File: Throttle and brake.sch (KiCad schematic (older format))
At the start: 9 parts, among them P2 Throttle Pedal, U1 Amplifier, U2 ADUC816

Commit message: version from flash drive
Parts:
- removed R3: Pot, symbol POT
- removed U2: ADUC816, symbol ADUC816
- added C? (x2): CP1, symbol CP1
- added P3: Pot connector, Connect:bornier3, symbol CONN_01X03
- added Q?: Q_PNP_BCE, symbol Q_PNP_BCE
- added R? (x2): R, symbol R
- added U2: Teensy_3.2, symbol Teensy_3.2
- 10k1, P2: footprint (none) -> Connect:bornier3
- 3P1: renamed from .2; footprint (none) -> Connect:bornier3
- 4P1: renamed from .; footprint (none) -> Connect:bornier4
- R1, R2: footprint (none) -> Resistors_SMD:R_1210_HandSoldering
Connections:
- net labels added: Brakesignal, GNDREF, Throttlesignal
- wire segments 47 -> 44
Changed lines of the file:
@@
 LIBS:contrib
 LIBS:valves
+LIBS:electric_car
 LIBS:Throttle and brake-cache
 EELAYER 25 0
@@
 $EndDescr
 $Comp
-L POT R3
-U 1 1 57F328A6
-P 3150 2000
-F 0 "R3" H 3150 1920 50  0000 C CNN
-F 1 "Pot" H 3150 2000 50  0000 C CNN
-F 2 "" H 3150 2000 50  0000 C CNN
-F 3 "" H 3150 2000 50  0000 C CNN
-	1    3150 2000
-	0    1    1    0
-$EndComp
-$Comp
 L R_Small R1
 U 1 1 57F33006
@@
 F 0 "R1" H 2280 3120 50  0000 L CNN
 F 1 "1k" H 2280 3060 50  0000 L CNN
-F 2 "" H 2250 3100 50  0000 C CNN
+F 2 "Resistors_SMD:R_1210_HandSoldering" H 2250 3100 50  0001 C CNN
 F 3 "" H 2250 3100 50  0000 C CNN
 	1    2250 3100
@@
 F 0 "R2" H 2280 3520 50  0000 L CNN
 F 1 "1k" H 2280 3460 50  0000 L CNN
-F 2 "" H 2250 3500 50  0000 C CNN
+F 2 "Resistors_SMD:R_1210_HandSoldering" H 2250 3500 50  0001 C CNN
 F 3 "" H 2250 3500 50  0000 C CNN
 	1    2250 3500
@@
 F 0 "10k1" H 1950 3270 50  0000 C CNN
 F 1 "POT" H 1950 3350 50  0000 C CNN
-F 2 "" H 1950 3350 50  0000 C CNN
+F 2 "Connect:bornier3" H 1950 3350 50  0001 C CNN
 F 3 "" H 1950 3350 50  0000 C CNN
 	1    1950 3350
@@
 F 0 "U1" H 3900 3500 50  0000 L CNN
 F 1 "Amplifier" H 3900 3050 50  0000 L CNN
-F 2 "" H 3950 3300 50  0000 C CNN
+F 2 "" H 3950 3300 50  0001 C CNN
 F 3 "" H 3950 3300 50  0000 C CNN
 	1    3950 3300
-	1    0    0    -1
-$EndComp
-$Comp
-L ADUC816 U2
-U 1 1 57F33F31
-P 7250 2800
-F 0 "U2" H 6300 4600 50  0000 L CNN
-F 1 "ADUC816" H 6300 4500 50  0000 L CNN
-F 2 "" H 7250 2600 50  0000 C CNN
-F 3 "" H 7250 2600 50  0000 C CNN
-	1    7250 2800
 	1    0    0    -1
 $EndComp
@@
 	1    0    0    -1
 $EndComp
-Wire Notes Line
-	3300 1750 3000 1750
-Wire Notes Line
-	3300 2250 3300 1750
-Wire Notes Line
-	3000 2250 3300 2250
-Wire Notes Line
-	3000 1750 3000 2250
 Connection ~ 2550 2850
 Wire Wire Line
 	3850 2850 3850 3000
-Wire Wire Line
-	5550 1600 6150 1600
-Wire Wire Line
-	5550 3300 5550 1600
-Wire Wire Line
-	4250 3300 5550 3300
-Wire Wire Line
-	5300 1500 6150 1500
-Wire Wire Line
-	5300 2000 5300 1500
-Wire Wire Line
-	3300 2000 5300 2000
 Connection ~ 1950 1650
 Connection ~ 1950 2850
@@
 	1950 3750 1950 3500
 Wire Wire Line
-	2550 3750 2250 3750
-Wire Wire Line
-	2250 3750 1950 3750
-Wire Wire Line
-	2550 3600 2550 3750
+	1950 3750 2550 3750
+Wire Wire Line
+	2550 3750 2550 3600
 Connection ~ 2550 3000
 Wire Wire Line
 	1950 2850 1950 3200
 Wire Wire Line
-	1650 2850 1950 2850
-Wire Wire Line
-	1950 2850 2550 2850
-Wire Wire Line
-	2550 2850 3850 2850
+	1650 2850 3850 2850
 Wire Wire Line
 	2550 2850 2550 3000
 Connection ~ 2250 3350
 Wire Wire Line
-	2250 3000 2550 3000
-Wire Wire Line
-	2550 3000 2800 3000
-Wire Wire Line
-	2250 3600 2550 3600
-Wire Wire Line
-	2550 3600 2800 3600
-Wire Wire Line
-	2250 3200 2250 3350
-Wire Wire Line
-	2250 3350 2250 3400
-Wire Wire Line
-	3150 2400 3150 2150
-Wire Wire Line
-	1950 2400 2550 2400
-Wire Wire Line
-	2550 2400 3150 2400
-Wire Wire Line
-	3150 1650 3150 1850
-Wire Wire Line
-	1650 1650 1950 1650
-Wire Wire Line
-	1950 1650 3150 1650
+	2250 3000 2800 3000
+Wire Wire Line
+	2250 3600 2800 3600
+Wire Wire Line
+	2250 3200 2250 3400
+Wire Wire Line
+	3150 2100 3150 2400
+Wire Wire Line
+	3150 2400 1950 2400
+Wire Wire Line
+	3150 1650 3150 1900
+Wire Wire Line
+	1650 1650 3150 1650
 Connection ~ 100  450
 $Comp
@@
 Jean, Fred. Euphraim
 $Comp
-L CONN_01X03 .2
+L CONN_01X03 3P1
 U 1 1 57F357A4
 P 4500 4850
-F 0 ".2" H 4500 5150 50  0000 C CNN
+F 0 "3P1" H 4500 5150 50  0000 C CNN
 F 1 "Lever" V 4600 4850 50  0000 C CNN
-F 2 "" H 4500 4850 50  0000 C CNN
+F 2 "Connect:bornier3" H 4500 4850 50  0001 C CNN
 F 3 "" H 4500 4850 50  0000 C CNN
 	1    4500 4850
@@
 	4250 4850 4300 4850
 $Comp
-L CONN_01X04 .
+L CONN_01X04 4P1
 U 1 1 580590EC
 P 2600 4850
-F 0 "." H 2600 5100 50  0000 C CNN
+F 0 "4P1" H 2600 5100 50  0000 C CNN
 F 1 "Ignition Switch" V 2700 4850 50  0000 C CNN
-F 2 "" H 2600 4850 50  0000 C CNN
+F 2 "Connect:bornier4" H 2600 4850 50  0001 C CNN
 F 3 "" H 2600 4850 50  0000 C CNN
 	1    2600 4850
@@
 F 0 "P2" H 3000 3500 35  0000 C CNN
 F 1 "Throttle Pedal" V 3100 3300 50  0000 C CNN
-F 2 "" H 3000 3300 50  0000 C CNN
+F 2 "Connect:bornier3" H 3000 3300 50  0001 C CNN
 F 3 "" H 3000 3300 50  0000 C CNN
 	1    3000 3300
@@
 $EndComp
 Wire Wire Line
-	2100 3350 2250 3350
-Wire Wire Line
-	2250 3350 2650 3350
+	2100 3350 2650 3350
 Wire Wire Line
 	2650 3350 2650 3550
@@
 Wire Wire Line
 	2800 3600 2800 3400
+$Comp
+L CONN_01X03 P3
+U 1 1 580ECAE0
+P 3350 2000
+F 0 "P3" H 3350 2200 50  0000 C CNN
+F 1 "Pot connector" V 3450 2000 50  0000 C CNN
+F 2 "Connect:bornier3" H 3350 2000 50  0001 C CNN
+F 3 "" H 3350 2000 50  0000 C CNN
+	1    3350 2000
+	1    0    0    -1
+$EndComp
+Wire Wire Line
+	3000 2000 3000 1500
+Connection ~ 3150 2000
+Wire Wire Line
+	3000 2000 3150 2000
+$Comp
+L Teensy_3.2 U2
+U 1 1 580EFC2E
+P 6700 2750
+F 0 "U2" H 6700 2600 39  0000 C CNN
+F 1 "Teensy_3.2" H 6700 3300 39  0000 C CNN
+F 2 "" H 6400 2300 39  0001 C CNN
+F 3 "" H 6400 2300 39  0000 C CNN
+	1    6700 2750
+	1    0    0    -1
+$EndComp
+Wire Wire Line
+	7650 2650 7400 2650
+Wire Wire Line
+	7650 1500 7650 2550
+Wire Wire Line
+	7650 2550 7400 2550
+$Comp
+L GNDREF #PWR07
+U 1 1 580F04E9
+P 5600 2150
+F 0 "#PWR07" H 5600 1900 50  0001 C CNN
+F 1 "GNDREF" H 5600 2000 50  0000 C CNN
+F 2 "" H 5600 2150 50  0000 C CNN
+F 3 "" H 5600 2150 50  0000 C CNN
+	1    5600 2150
+	1    0    0    -1
+$EndComp
+Text Label 3000 1500 0    60   ~ 0
+Brakesignal
+Text Label 7650 1500 0    60   ~ 0
+Brakesignal
+Text Label 4250 3300 0    60   ~ 0
+Throttlesignal
+Text Label 7650 2650 0    60   ~ 0
+Throttlesignal
+Wire Wire Line
+	6000 2050 5600 2050
+Wire Wire Line
+	5600 2050 5600 2150
+$Comp
+L CP1 C?
+U 1 1 58213AD5
+P 1750 5950
+F 0 "C?" H 1775 6050 50  0000 L CNN
+F 1 "CP1" H 1775 5850 50  0000 L CNN
+F 2 "" H 1750 5950 50  0000 C CNN
+F 3 "" H 1750 5950 50  0000 C CNN
+	1    1750 5950
+	1    0    0    -1
+$EndComp
+$Comp
+L Q_PNP_BCE Q?
+U 1 1 58214ECE
+P 3900 6000
+F 0 "Q?" H 4200 6050 50  0000 R CNN
+F 1 "Q_PNP_BCE" H 4500 5950 50  0000 R CNN
+F 2 "" H 4100 6100 50  0000 C CNN
+F 3 "" H 3900 6000 50  0000 C CNN
+	1    3900 6000
+	0    -1   -1   0
+$EndComp
+$Comp
+L CP1 C?
+U 1 1 58214F8D
+P 1800 6650
+F 0 "C?" H 1825 6750 50  0000 L CNN
+F 1 "CP1" H 1825 6550 50  0000 L CNN
+F 2 "" H 1800 6650 50  0000 C CNN
+F 3 "" H 1800 6650 50  0000 C CNN
+	1    1800 6650
+	1    0    0    -1
+$EndComp
+$Comp
+L R R?
+U 1 1 58215071
+P 2700 5900
+F 0 "R?" V 2780 5900 50  0000 C CNN
+F 1 "R" V 2700 5900 50  0000 C CNN
+F 2 "" V 2630 5900 50  0000 C CNN
+F 3 "" H 2700 5900 50  0000 C CNN
+	1    2700 5900
+	0    1    1    0
+$EndComp
+$Comp
+L R R?
+U 1 1 5821529C
+P 3200 5900
+F 0 "R?" H 3280 5900 50  0000 C CNN
+F 1 "R" V 3200 5900 50  0000 C CNN
+F 2 "" V 3130 5900 50  0000 C CNN
+F 3 "" H 3200 5900 50  0000 C CNN
+	1    3200 5900
+	0    1    1    0
+$EndComp
+Wire Wire Line
+	2850 5900 3050 5900
+Wire Wire Line
+	3350 5900 3700 5900
+Wire Wire Line
+	1750 5800 1750 5650
+Wire Wire Line
+	1300 5650 3400 5650
+Wire Wire Line
+	3400 5650 3400 5900
+Connection ~ 3400 5900
+Connection ~ 1750 5650
 $EndSCHEMATC

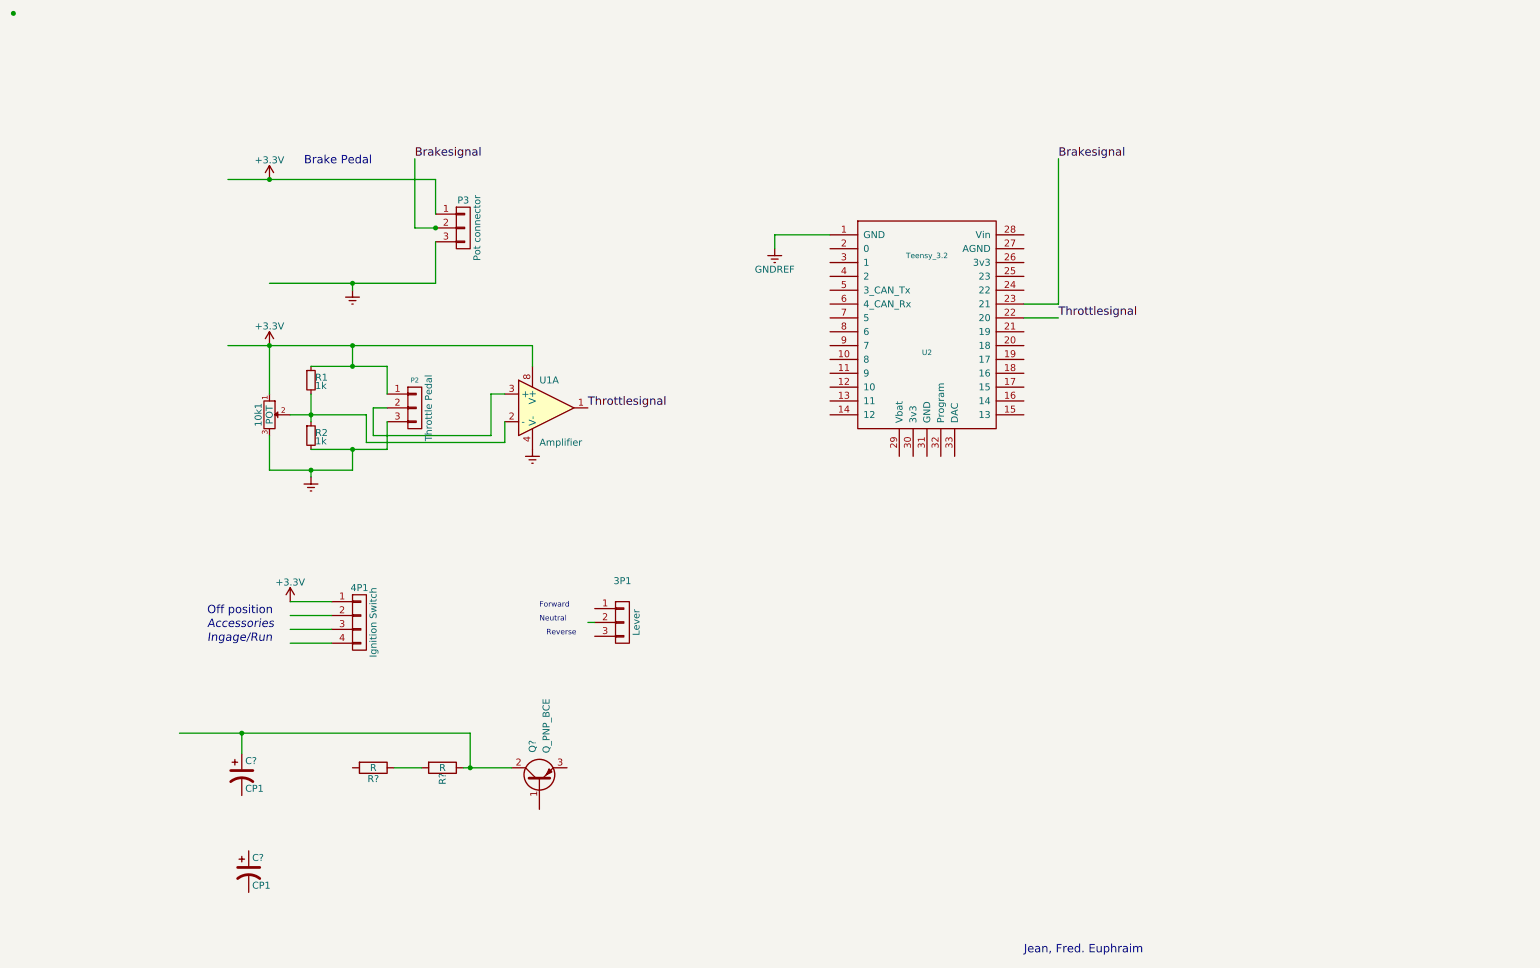
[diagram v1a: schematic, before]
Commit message: added hx711 and organised schematic
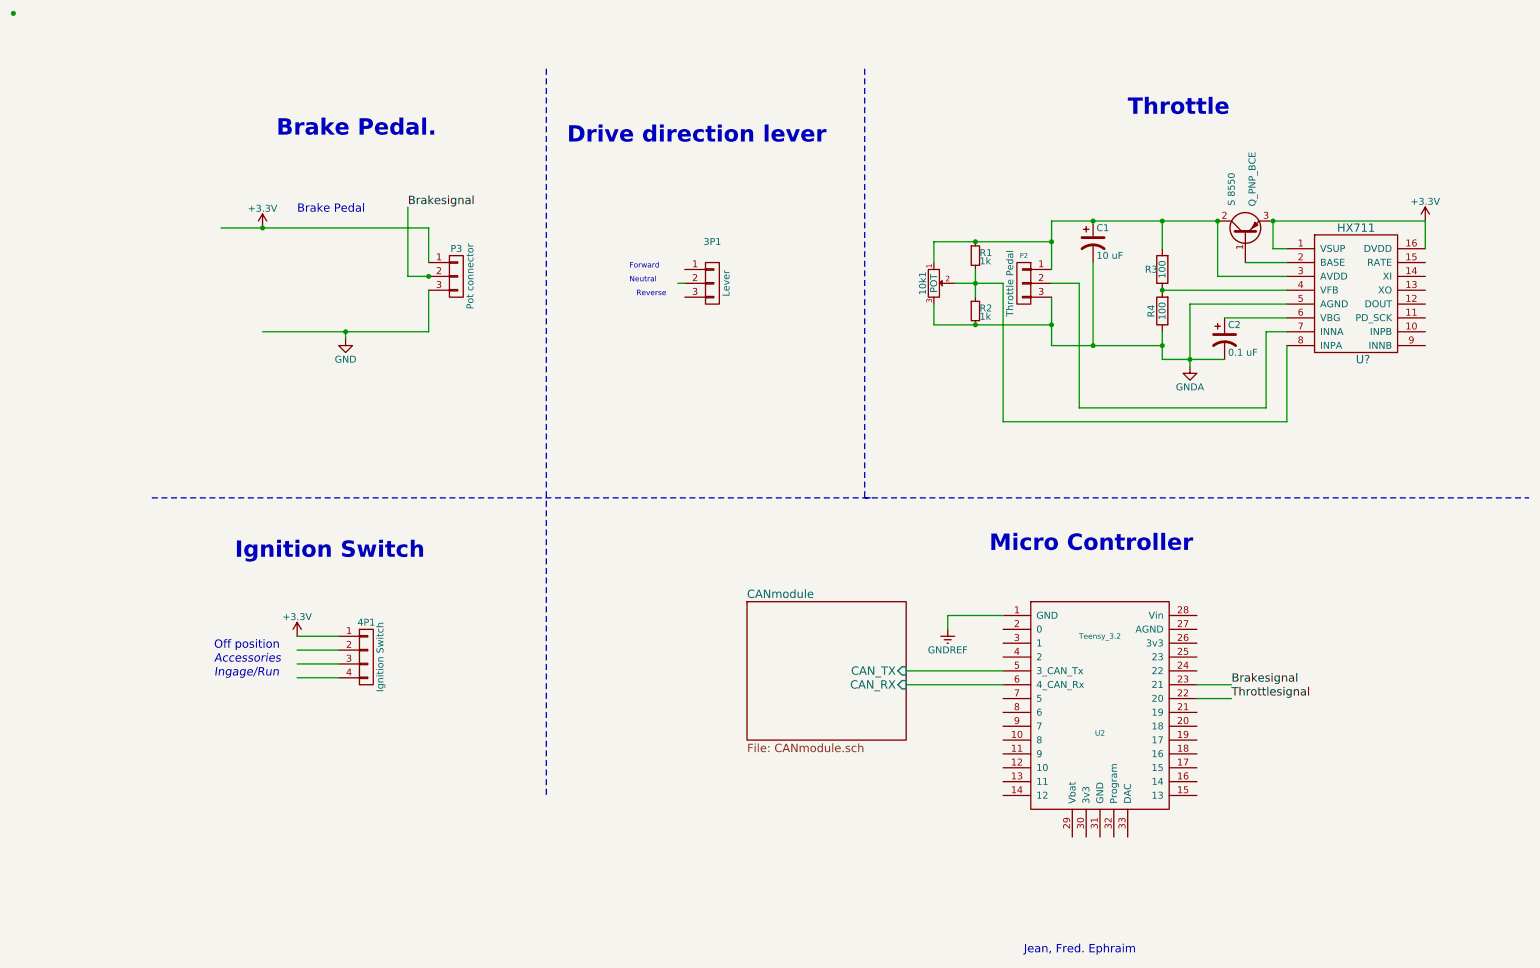
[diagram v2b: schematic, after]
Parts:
- removed U1: Amplifier, symbol LM358
- added U?: HX711, symbol HX711
- C1: renamed from C?; value CP1 -> 10 uF
- C2: renamed from C?; value CP1 -> 0.1 uF
- R3, R4: renamed from R?; value R -> 100
- gave numbers to parts that had none: 1
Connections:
- net labels added: GND, GNDA
- net labels removed: Earth
- wire segments 44 -> 51
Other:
- note added: "Brake Pedal.\n"
- note added: "Drive direction lever"
- note added: "Ignition Switch"
- note added: "Jean, Fred. Ephraim"
- note added: "Micro Controller"
- note added: "Throttle"
- note removed: "Jean, Fred. Euphraim"
- moved on the sheet: 10k1, 3P1, 4P1, C1, C2, P2, P3, R1, R2, R3, R4, S 8550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

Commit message: PCB layout
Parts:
- C101: renamed from C1; footprint (none) -> Capacitors_SMD:C_1210_HandSoldering
- C102: renamed from C2; footprint (none) -> Capacitors_SMD:C_1206_HandSoldering
- R101: renamed from R1; footprint Resistors_SMD:R_1210_HandSoldering -> Resistors_SMD:R_1206_HandSoldering
- R102: renamed from R2; footprint Resistors_SMD:R_1210_HandSoldering -> Resistors_SMD:R_1206_HandSoldering
- R103: renamed from R3; footprint (none) -> Resistors_SMD:R_1206_HandSoldering
- R104: renamed from R4; footprint (none) -> Resistors_SMD:R_1206_HandSoldering
- S101: renamed from S; footprint (none) -> TO_SOT_Packages_SMD:SOT-23_Handsoldering
- gave numbers to parts that had none: 1
- renumbered 10k1 to 10k101, 3P1 to 3P101, 4P1 to 4P101, P3 to P101, P2 to P102, U2 to U101
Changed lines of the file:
@@
 $EndDescr
 $Comp
-L R_Small R1
+L R_Small R101
 U 1 1 57F33006
 P 7050 2200
-F 0 "R1" H 7080 2220 50  0000 L CNN
+F 0 "R101" H 7080 2220 50  0000 L CNN
 F 1 "1k" H 7080 2160 50  0000 L CNN
-F 2 "Resistors_SMD:R_1210_HandSoldering" H 7050 2200 50  0001 C CNN
+F 2 "Resistors_SMD:R_1206_HandSoldering" H 7050 2200 50  0001 C CNN
 F 3 "" H 7050 2200 50  0000 C CNN
 	1    7050 2200
@@
 $EndComp
 $Comp
-L R_Small R2
+L R_Small R102
 U 1 1 57F33A40
 P 7050 2600
-F 0 "R2" H 7080 2620 50  0000 L CNN
+F 0 "R102" H 7080 2620 50  0000 L CNN
 F 1 "1k" H 7080 2560 50  0000 L CNN
-F 2 "Resistors_SMD:R_1210_HandSoldering" H 7050 2600 50  0001 C CNN
+F 2 "Resistors_SMD:R_1206_HandSoldering" H 7050 2600 50  0001 C CNN
 F 3 "" H 7050 2600 50  0000 C CNN
 	1    7050 2600
@@
 $EndComp
 $Comp
-L POT 10k1
+L POT 10k101
 U 1 1 57F33B0B
 P 6750 2400
-F 0 "10k1" H 6750 2320 50  0000 C CNN
+F 0 "10k101" H 6750 2320 50  0000 C CNN
 F 1 "POT" H 6750 2400 50  0000 C CNN
 F 2 "Connect:bornier3" H 6750 2400 50  0001 C CNN
@@
 Brake Pedal
 $Comp
-L +3.3V #PWR04
+L +3.3V #PWR01
 U 1 1 57F357A5
 P 1900 2000
-F 0 "#PWR04" H 1900 1850 50  0001 C CNN
+F 0 "#PWR01" H 1900 1850 50  0001 C CNN
 F 1 "+3.3V" H 1900 2140 50  0000 C CNN
 F 2 "" H 1900 2000 50  0000 C CNN
@@
 Jean, Fred. Ephraim
 $Comp
-L CONN_01X03 3P1
+L CONN_01X03 3P101
 U 1 1 57F357A4
 P 5150 2400
-F 0 "3P1" H 5150 2700 50  0000 C CNN
+F 0 "3P101" H 5150 2700 50  0000 C CNN
 F 1 "Lever" V 5250 2400 50  0000 C CNN
 F 2 "Connect:bornier3" H 5150 2400 50  0001 C CNN
@@
 	4900 2400 4950 2400
 $Comp
-L CONN_01X04 4P1
+L CONN_01X04 4P101
 U 1 1 580590EC
 P 2650 5100
-F 0 "4P1" H 2650 5350 50  0000 C CNN
+F 0 "4P101" H 2650 5350 50  0000 C CNN
 F 1 "Ignition Switch" V 2750 5100 50  0000 C CNN
 F 2 "Connect:bornier4" H 2650 5100 50  0001 C CNN
@@
 	2450 4950 2150 4950
 $Comp
-L +3.3V #PWR06
+L +3.3V #PWR02
 U 1 1 58059B66
 P 2150 4950
-F 0 "#PWR06" H 2150 4800 50  0001 C CNN
+F 0 "#PWR02" H 2150 4800 50  0001 C CNN
 F 1 "+3.3V" H 2150 5090 50  0000 C CNN
 F 2 "" H 2150 4950 50  0000 C CNN
@@
 Ingage/Run
 $Comp
-L CONN_01X03 P2
+L CONN_01X03 P102
 U 1 1 5805A8E1
 P 7400 2400
-F 0 "P2" H 7400 2600 35  0000 C CNN
+F 0 "P102" H 7400 2600 35  0000 C CNN
 F 1 "Throttle Pedal" V 7500 2400 50  0000 C CNN
 F 2 "Connect:bornier3" H 7400 2400 50  0001 C CNN
@@
 	7600 2500 7600 2850
 $Comp
-L CONN_01X03 P3
+L CONN_01X03 P101
 U 1 1 580ECAE0
 P 3300 2350
-F 0 "P3" H 3300 2550 50  0000 C CNN
+F 0 "P101" H 3300 2550 50  0000 C CNN
 F 1 "Pot connector" V 3400 2350 50  0000 C CNN
 F 2 "Connect:bornier3" H 3300 2350 50  0001 C CNN
@@
 	2950 2350 3100 2350
 $Comp
-L Teensy_3.2 U2
+L Teensy_3.2 U101
 U 1 1 580EFC2E
 P 7950 5500
-F 0 "U2" H 7950 5350 39  0000 C CNN
+F 0 "U101" H 7950 5350 39  0000 C CNN
 F 1 "Teensy_3.2" H 7950 6050 39  0000 C CNN
 F 2 "" H 7650 5050 39  0001 C CNN
@@
 	8650 5300 8900 5300
 $Comp
-L GNDREF #PWR07
+L GNDREF #PWR03
 U 1 1 580F04E9
 P 6850 4900
-F 0 "#PWR07" H 6850 4650 50  0001 C CNN
+F 0 "#PWR03" H 6850 4650 50  0001 C CNN
 F 1 "GNDREF" H 6850 4750 50  0000 C CNN
 F 2 "" H 6850 4900 50  0000 C CNN
@@
 	6850 4800 6850 4900
 $Comp
-L CP1 C1
+L CP1 C101
 U 1 1 58213AD5
 P 7900 2100
-F 0 "C1" H 7925 2200 50  0000 L CNN
+F 0 "C101" H 7925 2200 50  0000 L CNN
 F 1 "10 uF" H 7925 2000 50  0000 L CNN
-F 2 "" H 7900 2100 50  0000 C CNN
+F 2 "Capacitors_SMD:C_1210_HandSoldering" H 7900 2100 50  0001 C CNN
 F 3 "" H 7900 2100 50  0000 C CNN
 	1    7900 2100
@@
 $EndComp
 $Comp
-L Q_PNP_BCE S
+L Q_PNP_BCE S101
 U 1 1 58214ECE
 P 9000 2050
-F 0 "S 8550" H 9450 2150 50  0000 R CNN
+F 0 "S101" H 9450 2150 50  0000 R CNN
 F 1 "Q_PNP_BCE" H 9600 2000 50  0000 R CNN
-F 2 "" H 9200 2150 50  0000 C CNN
+F 2 "TO_SOT_Packages_SMD:SOT-23_Handsoldering" H 9200 2150 50  0001 C CNN
 F 3 "" H 9000 2050 50  0000 C CNN
 	1    9000 2050
@@
 $EndComp
 $Comp
-L CP1 C2
+L CP1 C102
 U 1 1 58214F8D
 P 8850 2800
-F 0 "C2" H 8875 2900 50  0000 L CNN
+F 0 "C102" H 8875 2900 50  0000 L CNN
 F 1 "0.1 uF" H 8875 2700 50  0000 L CNN
-F 2 "" H 8850 2800 50  0000 C CNN
+F 2 "Capacitors_SMD:C_1206_HandSoldering" H 8850 2800 50  0001 C CNN
 F 3 "" H 8850 2800 50  0000 C CNN
 	1    8850 2800
@@
 $EndComp
 $Comp
-L R R4
+L R R104
 U 1 1 58215071
 P 8400 2600
-F 0 "R4" V 8480 2600 50  0000 C CNN
+F 0 "R104" V 8480 2600 50  0000 C CNN
 F 1 "100" V 8400 2600 50  0000 C CNN
-F 2 "" V 8330 2600 50  0000 C CNN
+F 2 "Resistors_SMD:R_1206_HandSoldering" V 8330 2600 50  0001 C CNN
 F 3 "" H 8400 2600 50  0000 C CNN
 	1    8400 2600
@@
 $EndComp
 $Comp
-L R R3
+L R R103
 U 1 1 5821529C
 P 8400 2300
-F 0 "R3" H 8480 2300 50  0000 C CNN
+F 0 "R103" H 8480 2300 50  0000 C CNN
 F 1 "100" V 8400 2300 50  0000 C CNN
-F 2 "" V 8330 2300 50  0000 C CNN
+F 2 "Resistors_SMD:R_1206_HandSoldering" V 8330 2300 50  0001 C CNN
 F 3 "" H 8400 2300 50  0000 C CNN
 	1    8400 2300
@@
 $EndComp
 $Comp
-L HX711 U?
+L HX711 U102
 U 1 1 5821646F
 P 9800 2450
-F 0 "U?" H 9850 1950 60  0000 C CNN
+F 0 "U102" H 9850 1950 60  0000 C CNN
 F 1 "HX711" H 9800 2900 60  0000 C CNN
-F 2 "" H 9650 2100 60  0000 C CNN
+F 2 "" H 9650 2100 60  0001 C CNN
 F 3 "" H 9650 2100 60  0000 C CNN
 	1    9800 2450
@@
 	9300 3400 9300 2850
 $Comp
-L GND #PWR?
+L GND #PWR04
 U 1 1 5821A789
 P 2500 2800
-F 0 "#PWR?" H 2500 2550 50  0001 C CNN
+F 0 "#PWR04" H 2500 2550 50  0001 C CNN
 F 1 "GND" H 2500 2650 50  0000 C CNN
 F 2 "" H 2500 2800 50  0000 C CNN
@@
 Connection ~ 8400 2850
 $Comp
-L GNDA #PWR?
+L GNDA #PWR05
 U 1 1 5821C10E
 P 8600 3000
-F 0 "#PWR?" H 8600 2750 50  0001 C CNN
+F 0 "#PWR05" H 8600 2750 50  0001 C CNN
 F 1 "GNDA" H 8600 2850 50  0000 C CNN
 F 2 "" H 8600 3000 50  0000 C CNN
@@
 Micro Controller
 $Comp
-L +3.3V #PWR?
+L +3.3V #PWR06
 U 1 1 5821EF0E
 P 10300 1950
-F 0 "#PWR?" H 10300 1800 50  0001 C CNN
+F 0 "#PWR06" H 10300 1800 50  0001 C CNN
 F 1 "+3.3V" H 10300 2090 50  0000 C CNN
 F 2 "" H 10300 1950 50  0000 C CNN
